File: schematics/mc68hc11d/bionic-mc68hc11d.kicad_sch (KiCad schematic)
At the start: 5 parts, among them J1 Bionic-P135, J2 Bionic-P245, U1 MC68HC11D0P, U3 11AA010-I/TO

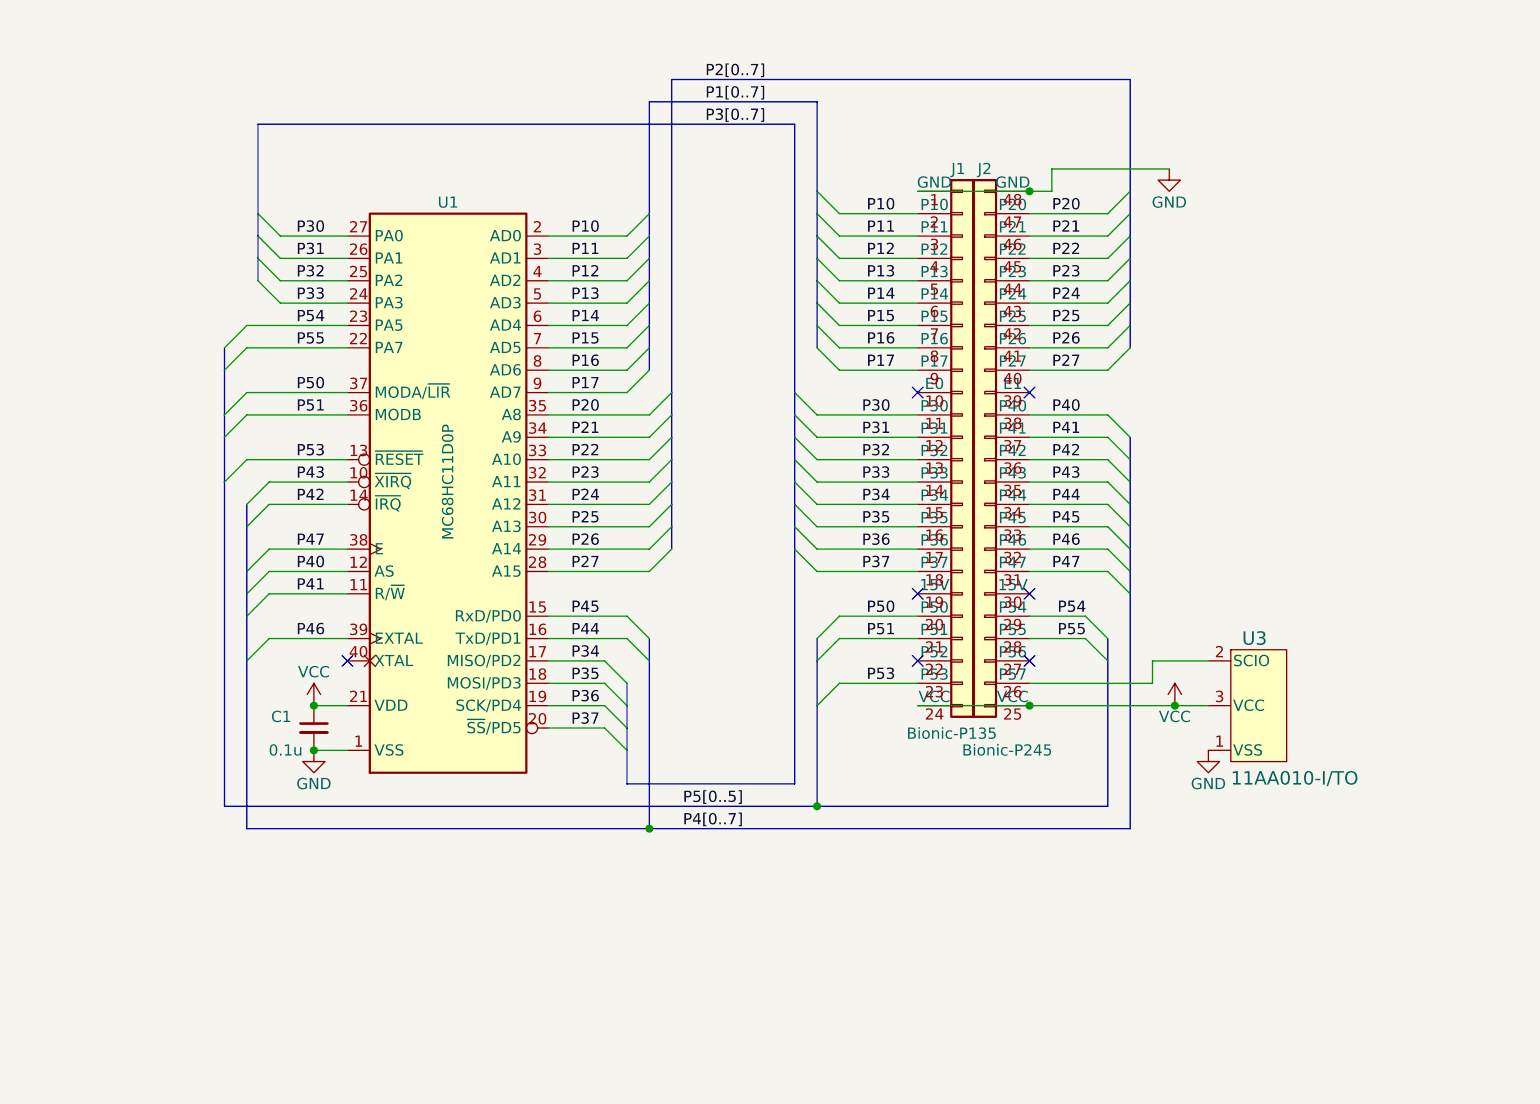
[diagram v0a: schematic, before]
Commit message: [MC68HC11D] Update schematics
Connect PAx and PDx
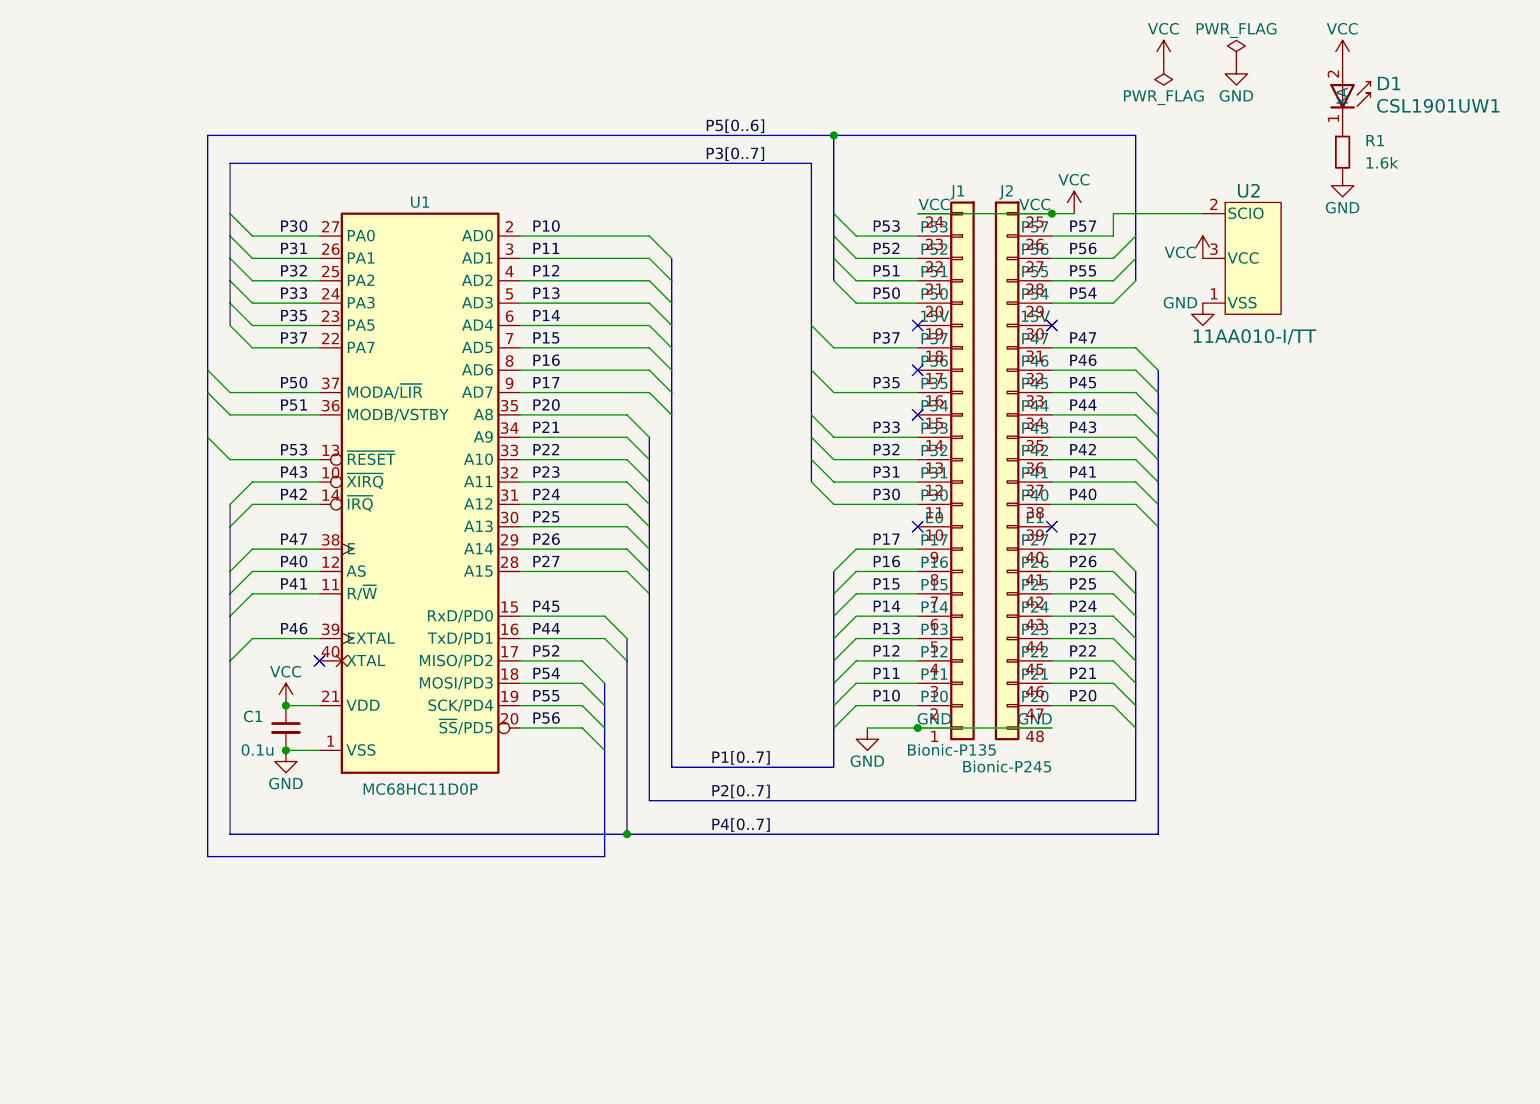
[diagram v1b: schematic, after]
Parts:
- removed U3: 11AA010-I/TO, TO-92_MC_MCH, symbol 0-LocalLibrary:11AA010-I_TO
- added D1: CSL1901UW1, 0-LocalLibrary:LED_CSL1901UW1_ROM, symbol 0-LocalLibrary:CSL1901UW1
- added R1: 1.6k, Resistor_SMD:R_0603_1608Metric_Pad0.98x0.95mm_HandSolder, symbol Device:R_Small
- added U2: 11AA010-I/TT, 0-LocalLibrary:SOT-23_MC_MCH-M, symbol 0-LocalLibrary:11AA010-I_TT
- C1: footprint Capacitor_THT:C_Disc_D3.4mm_W2.1mm_P2.50mm -> Capacitor_SMD:C_0603_1608Metric_Pad1.08x0.95mm_HandSolder
- J1: footprint connector:Bionic-P135_Vertical -> 0-LocalLibrary:Bionic-P135_Vertical
- J2: footprint connector:Bionic-P245_Vertical -> 0-LocalLibrary:Bionic-P245_Vertical
- U1: footprint Package_DIP:DIP-40_W15.24mm -> 0-LocalLibrary:DIP-40_W15.24mm_Socket
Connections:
- net GND: now also R1.2, U2.1 (VSS)
- net P35: now also U1.23 (PA5); no longer U1.18 (MOSI/PD3)
- net P37: now also U1.22 (PA7); no longer U1.20 (~{SS}/PD5)
- net P54: now also U1.18 (MOSI/PD3); no longer U1.23 (PA5)
- net P55: now also U1.19 (SCK/PD4); no longer U1.22 (PA7)
- net VCC: now also D1.2 (A), U2.3 (VCC)
- net P52: now reaches J1.22 (P52)
- net P52: now also U1.17 (MISO/PD2)
- net P57: now reaches J2.26 (P57)
- net P57: now also U2.2 (SCIO)
- net P56: now reaches J2.27 (P56)
- net P56: now also U1.20 (~{SS}/PD5)
- net P34: no longer names the net of J1.15 (P34)
- net P34: no longer U1.17 (MISO/PD2)
- net P36: no longer names the net of J1.17 (P36)
- net P36: no longer U1.19 (SCK/PD4)
- new net: D1.1 (K), R1.1
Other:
- moved on the sheet: C1

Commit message: [MC68xx] Read control signals as bus
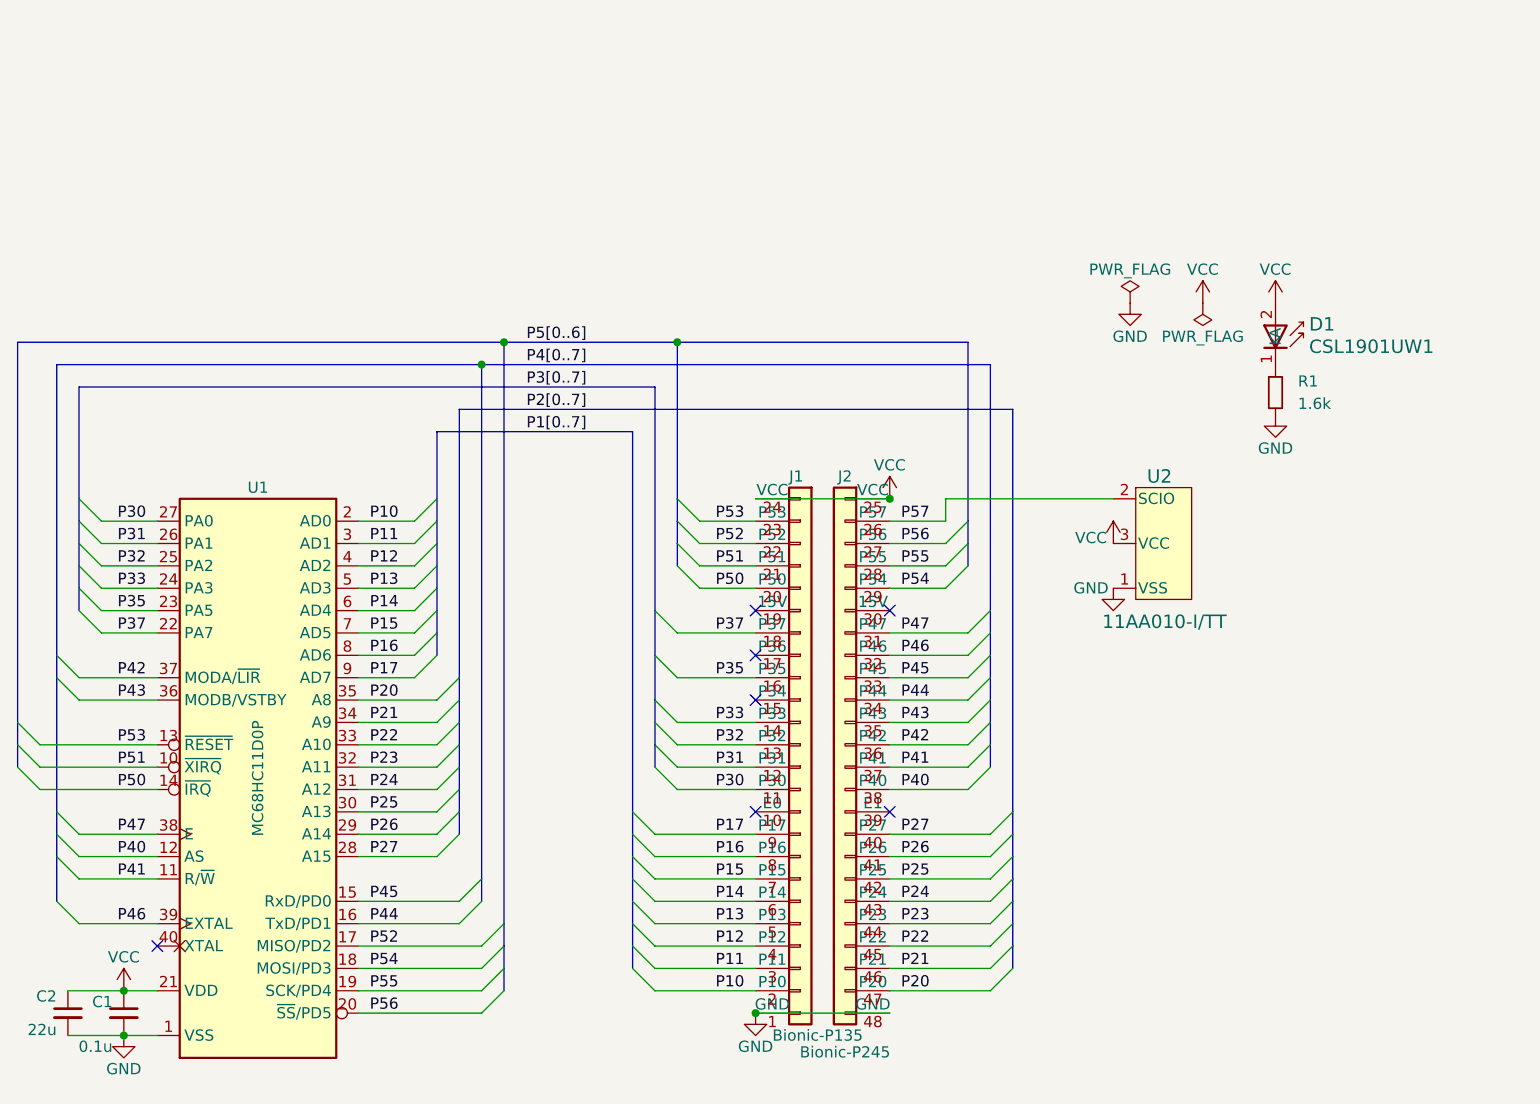
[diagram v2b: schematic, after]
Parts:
- added C2: 22u, Capacitor_SMD:C_0603_1608Metric_Pad1.08x0.95mm_HandSolder, symbol Device:C_Small
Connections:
- net GND: now also C2.2
- net P42: now also U1.37 (MODA/~{LIR}); no longer U1.14 (~{IRQ})
- net P43: now also U1.36 (MODB/VSTBY); no longer U1.10 (~{XIRQ})
- net P50: now also U1.14 (~{IRQ}); no longer U1.37 (MODA/~{LIR})
- net P51: now also U1.10 (~{XIRQ}); no longer U1.36 (MODB/VSTBY)
- net VCC: now also C2.1
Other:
- moved on the sheet: C1, D1, J1, J2, R1, U1, U2

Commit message: [MC68HC11D] Fix EEPROM pinout
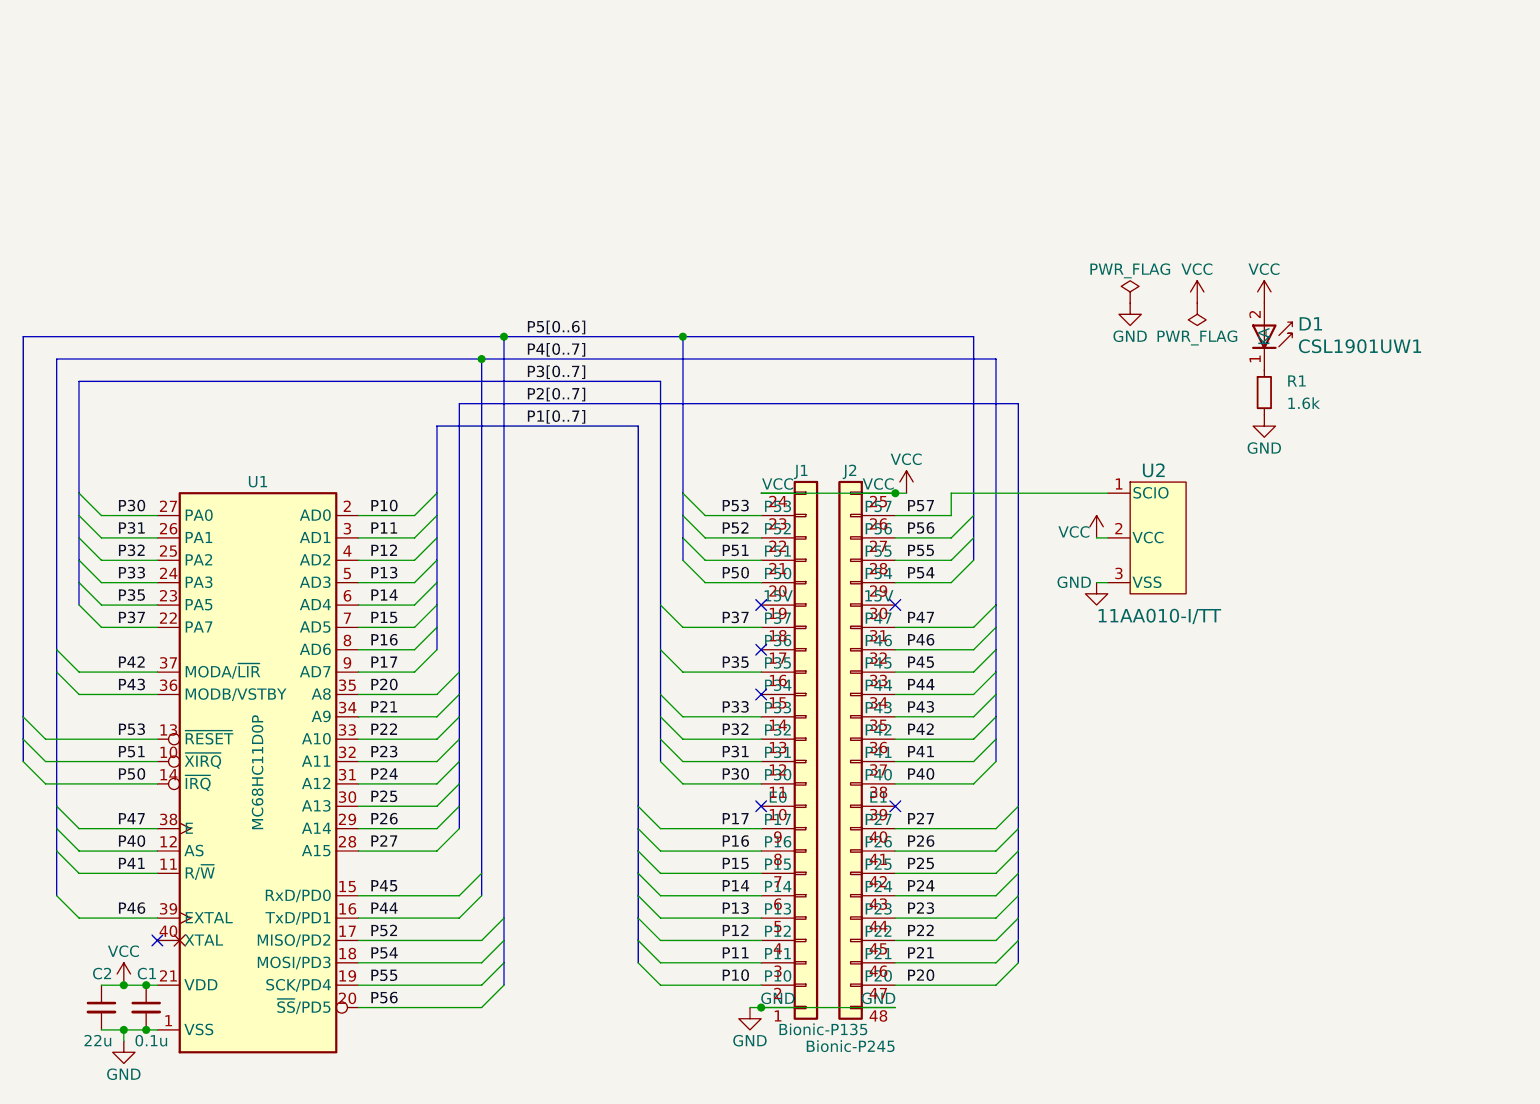
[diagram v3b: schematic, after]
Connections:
- net GND: now also U2.3 (VSS); no longer U2.1 (VSS)
- net P57: now also U2.1 (SCIO); no longer U2.2 (SCIO)
- net VCC: now also U2.2 (VCC); no longer U2.3 (VCC)
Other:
- moved on the sheet: C1, C2, D1, J1, J2, R1, U1, U2

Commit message: [schematics] Update LED footprint
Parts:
- D1: footprint 0-LocalLibrary:LED_CSL1901UW1_ROM -> 0-LocalLibrary:LED_CSL1901UW1_ROM-M

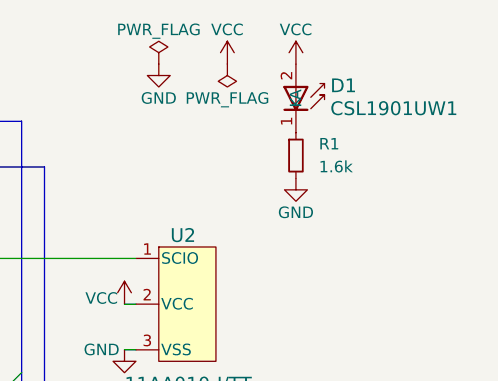
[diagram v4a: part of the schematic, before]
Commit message: [MC68HC11D] Cleanup schematics
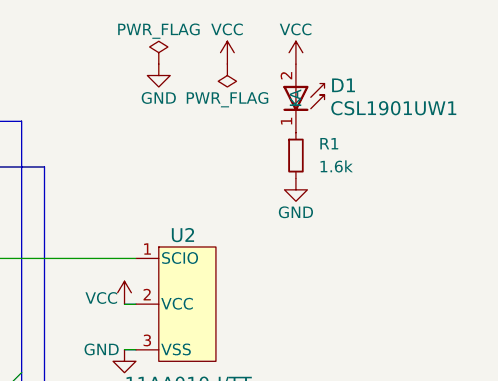
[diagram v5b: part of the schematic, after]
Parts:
- D1: footprint 0-LocalLibrary:LED_CSL1901UW1_ROM-M -> rhom:LED_CSL1901UW1_ROM-M; symbol 0-LocalLibrary:CSL1901UW1 -> rhom:CSL1901UW1
- J1: footprint 0-LocalLibrary:Bionic-P135_Vertical -> bionic:Bionic-P135_Vertical; symbol 0-LocalLibrary:Bionic-P135 -> bionic:Bionic-P135
- J2: footprint 0-LocalLibrary:Bionic-P245_Vertical -> bionic:Bionic-P245_Vertical; symbol 0-LocalLibrary:Bionic-P245 -> bionic:Bionic-P245
- U1: footprint 0-LocalLibrary:DIP-40_W15.24mm_Socket -> bionic:DIP-40_W15.24mm_Socket; symbol 0-LocalLibrary:MC68HC11D0P -> cpu:MC68HC11D0P
- U2: footprint 0-LocalLibrary:SOT-23_MC_MCH-M -> microchip:SOT-23_MC_MCH-M; symbol 0-LocalLibrary:11AA010-I_TT -> microchip:11AA010-I_TT
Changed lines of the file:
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@@
 	)
 	(symbol
-		(lib_id "0-LocalLibrary:Bionic-P245")
+		(lib_id "bionic:Bionic-P245")
 		(at 157.48 107.95 0)
 		(unit 1)
@@
 			)
 		)
-		(property "Footprint" "0-LocalLibrary:Bionic-P245_Vertical"
+		(property "Footprint" "bionic:Bionic-P245_Vertical"
 			(at 158.75 143.51 0)
 			(effects
@@
 			)
 		)
-		(property "Description" ""
+		(property "Description" "Generic connector, single row, 01x24, script generated (kicad-library-utils/schlib/autogen/connector/)"
 			(at 157.48 107.95 0)
 			(effects
@@
 	)
 	(symbol
-		(lib_id "0-LocalLibrary:MC68HC11D0P")
+		(lib_id "cpu:MC68HC11D0P")
 		(at 86.36 110.49 0)
 		(unit 1)
@@
 			)
 		)
-		(property "Footprint" "0-LocalLibrary:DIP-40_W15.24mm_Socket"
+		(property "Footprint" "bionic:DIP-40_W15.24mm_Socket"
 			(at 87.63 144.78 0)
 			(effects
@@
 			)
 		)
-		(property "Description" ""
+		(property "Description" "8-bit General Purpose Microprocessor, DIP-40"
 			(at 86.36 110.49 0)
 			(effects
@@
 	)
 	(symbol
-		(lib_id "0-LocalLibrary:11AA010-I_TT")
+		(lib_id "microchip:11AA010-I_TT")
 		(at 185.42 78.74 0)
 		(unit 1)
@@
 			)
 		)
-		(property "Footprint" "0-LocalLibrary:SOT-23_MC_MCH-M"
+		(property "Footprint" "microchip:SOT-23_MC_MCH-M"
 			(at 187.96 96.52 0)
 			(effects
@@
 			)
 		)
-		(property "Description" ""
+		(property "Description" "UNI/O Serial EEPROM (1Kbit)"
 			(at 185.42 78.74 0)
 			(effects
@@
 	)
 	(symbol
-		(lib_id "0-LocalLibrary:Bionic-P135")
+		(lib_id "bionic:Bionic-P135")
 		(at 148.59 107.95 0)
 		(unit 1)
@@
 			)
 		)
-		(property "Footprint" "0-LocalLibrary:Bionic-P135_Vertical"
+		(property "Footprint" "bionic:Bionic-P135_Vertical"
 			(at 149.86 143.51 0)
 			(effects
@@
 			)
 		)
-		(property "Description" ""
+		(property "Description" "Generic connector, single row, 01x24, script generated (kicad-library-utils/schlib/autogen/connector/)"
 			(at 148.59 107.95 0)
 			(effects
@@
 	)
 	(symbol
-		(lib_id "0-LocalLibrary:CSL1901UW1")
+		(lib_id "rhom:CSL1901UW1")
 		(at 200.66 58.42 270)
 		(unit 1)
@@
 		(fields_autoplaced yes)
 		(property "Reference" "D1"
-			(at 204.47 60.833 90)
+			(at 204.47 60.8329 90)
 			(effects
 				(font
@@
 		)
 		(property "Value" "CSL1901UW1"
-			(at 204.47 63.373 90)
+			(at 204.47 63.3729 90)
 			(effects
 				(font
@@
 			)
 		)
-		(property "Footprint" "0-LocalLibrary:LED_CSL1901UW1_ROM-M"
+		(property "Footprint" "rhom:LED_CSL1901UW1_ROM-M"
 			(at 191.77 62.23 0)
 			(effects
@@
 			)
 		)
-		(property "Description" ""
+		(property "Description" "Red LED (Low Current Emission, SMD)"
 			(at 200.66 58.42 0)
 			(effects
